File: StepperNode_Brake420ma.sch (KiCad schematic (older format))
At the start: 2 parts

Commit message: Update gimbal and brake MLP position sensor interfaces
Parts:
- added C? (x2): 100nF, symbol C
- added C? (x2): 1uF, symbol C
- added D? (x2): 1N4148, symbol D
- added U? (x2): RCV420JP, symbol RCV420JP
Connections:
- net labels added: +24V_A, BRAKE_MLP1_420MA, BRAKE_MLP2_420MA, GNDA
- wire segments 0 -> 20
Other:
- note added: "Original Author: SafetyLok"
- note added: "rLoop - Stepper Node\nBrake MLP 4-20 Interface\n"

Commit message: Update DAC's and routed gimbal position to MCU direct.
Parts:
- removed C? (x2): 100nF, symbol C
- removed C? (x2): 1uF, symbol C
- removed U? (x2): RCV420JP, symbol RCV420JP
- added C? (x2): C_100nF_50V, RLOOP_FOOTPRINTS:rLoop_C_0603, symbol C_100nF_50V
- added C? (x2): C_1uF_50V, RLOOP_FOOTPRINTS:rLoop_C_0603, symbol C_1uF_50V
- added R? (x2): 1.7K, RLOOP_FOOTPRINTS:rLoop_R_0603, symbol 1.7K
- added R? (x2): 3.3K, RLOOP_FOOTPRINTS:rLoop_R_0603, symbol 3.3K
- added U? (x2): RCV420JP, symbol RCV420JP
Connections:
- net labels added: BRAKE1_MLP_3V
- net labels removed: BRAKE1_MLP, BRAKE2_MLP
- wire segments 20 -> 22

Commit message: First Revision -
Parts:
- removed D? (x2): 1N4148, symbol D
- removed P? (x2): CONN_01X04-2XMNT, symbol CONN_01X04-2XMNT
- added D3, D4: BZX84C3V6LT1G, RLOOP_FOOTPRINTS:rLoop_SOT23, symbol BZX84C3V6LT1G
- added D5, D6: BAS16,215, RLOOP_FOOTPRINTS:rLoop_SOT23, symbol BAS16,215
- added P12: TE_640456-8, RLOOP_FOOTPRINTS:rLoop_TE640456-8, symbol TE_640456-8
- gave numbers to parts that had none: 10
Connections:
- net labels added: BRAKE2_MLP_3V
- wire segments 22 -> 25
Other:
- note added: "LHS/RHS Brake Interface Board\n4-20ma"
- note removed: "LHS Brake Interface Board\n4-20ma"
- note removed: "RHS Brake Interface Board\n4-20ma"

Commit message: Update per design review.
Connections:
- wire segments 25 -> 30
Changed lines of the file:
@@
 Wire Wire Line
 	10700 2600 11350 2600
+$Comp
+L GNDA #PWR?
+U 1 1 575D1FD8
+P 11300 3300
+F 0 "#PWR?" H 11300 3050 50  0001 C CNN
+F 1 "GNDA" H 11300 3150 50  0000 C CNN
+F 2 "" H 11300 3300 50  0000 C CNN
+F 3 "" H 11300 3300 50  0000 C CNN
+	1    11300 3300
+	1    0    0    -1
+$EndComp
+Wire Wire Line
+	11350 2800 11300 2800
+Wire Wire Line
+	11300 2800 11300 3300
+Wire Wire Line
+	11350 3100 11300 3100
+Connection ~ 11300 3100
+Wire Wire Line
+	11350 3000 11300 3000
+Connection ~ 11300 3000
+Wire Wire Line
+	11350 2900 11300 2900
+Connection ~ 11300 2900
 $EndSCHEMATC

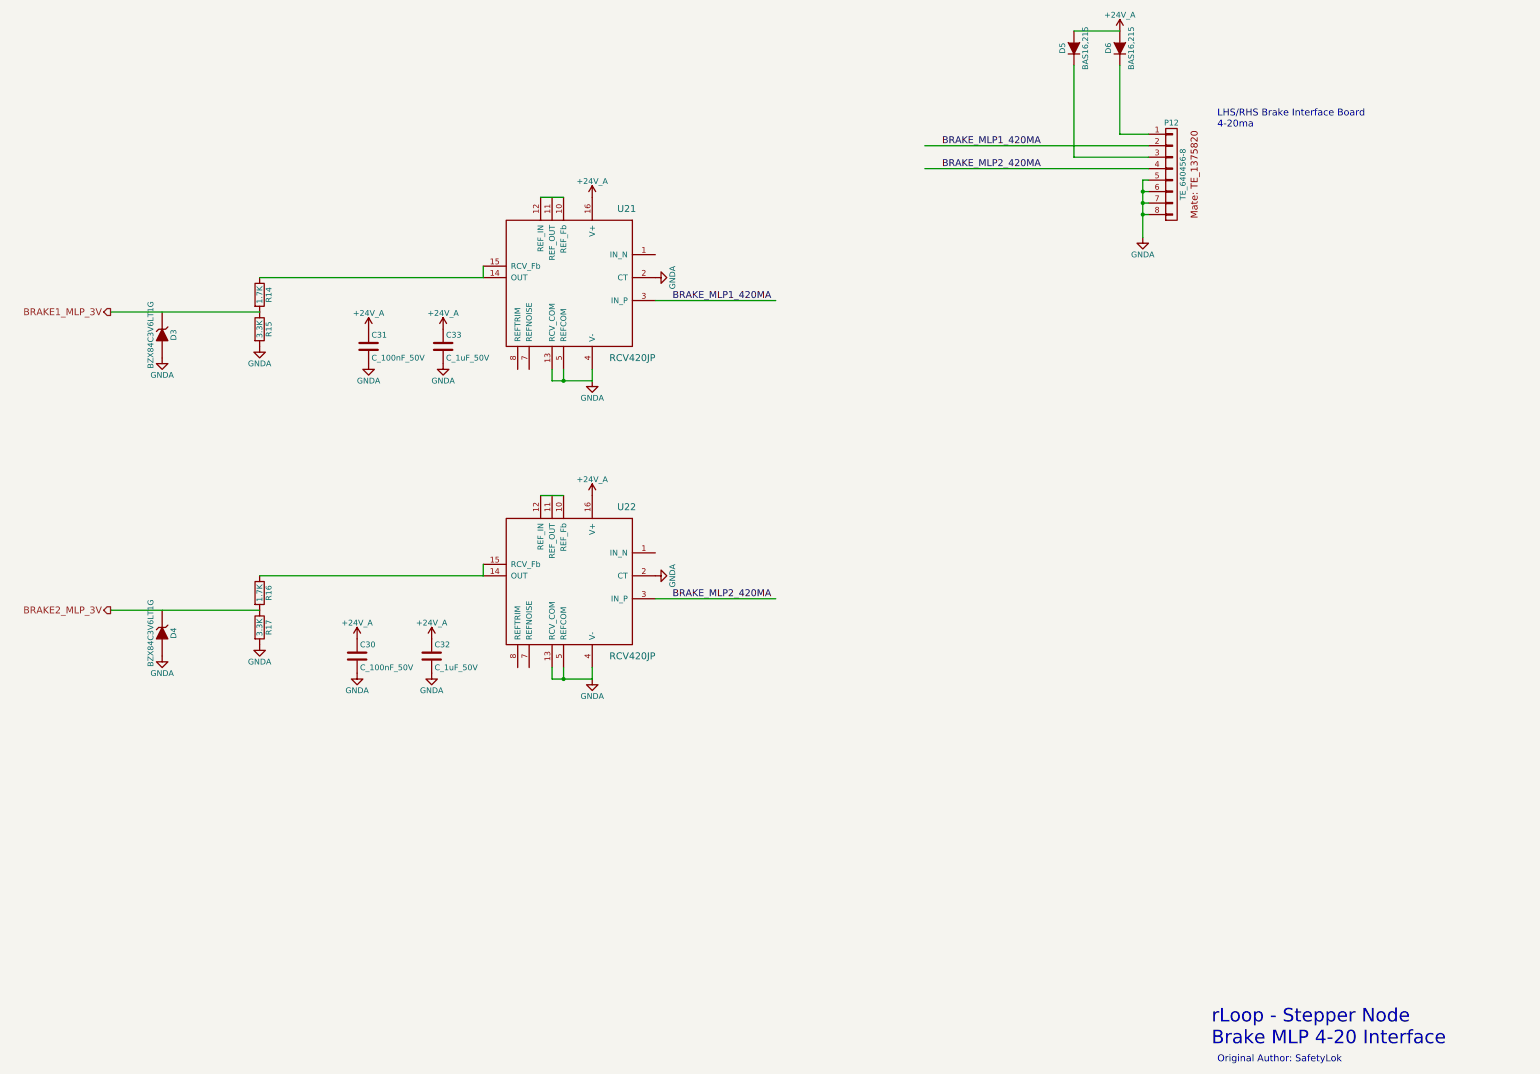
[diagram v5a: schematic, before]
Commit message: Fix most ERC warnings (non-connected pins, etc)
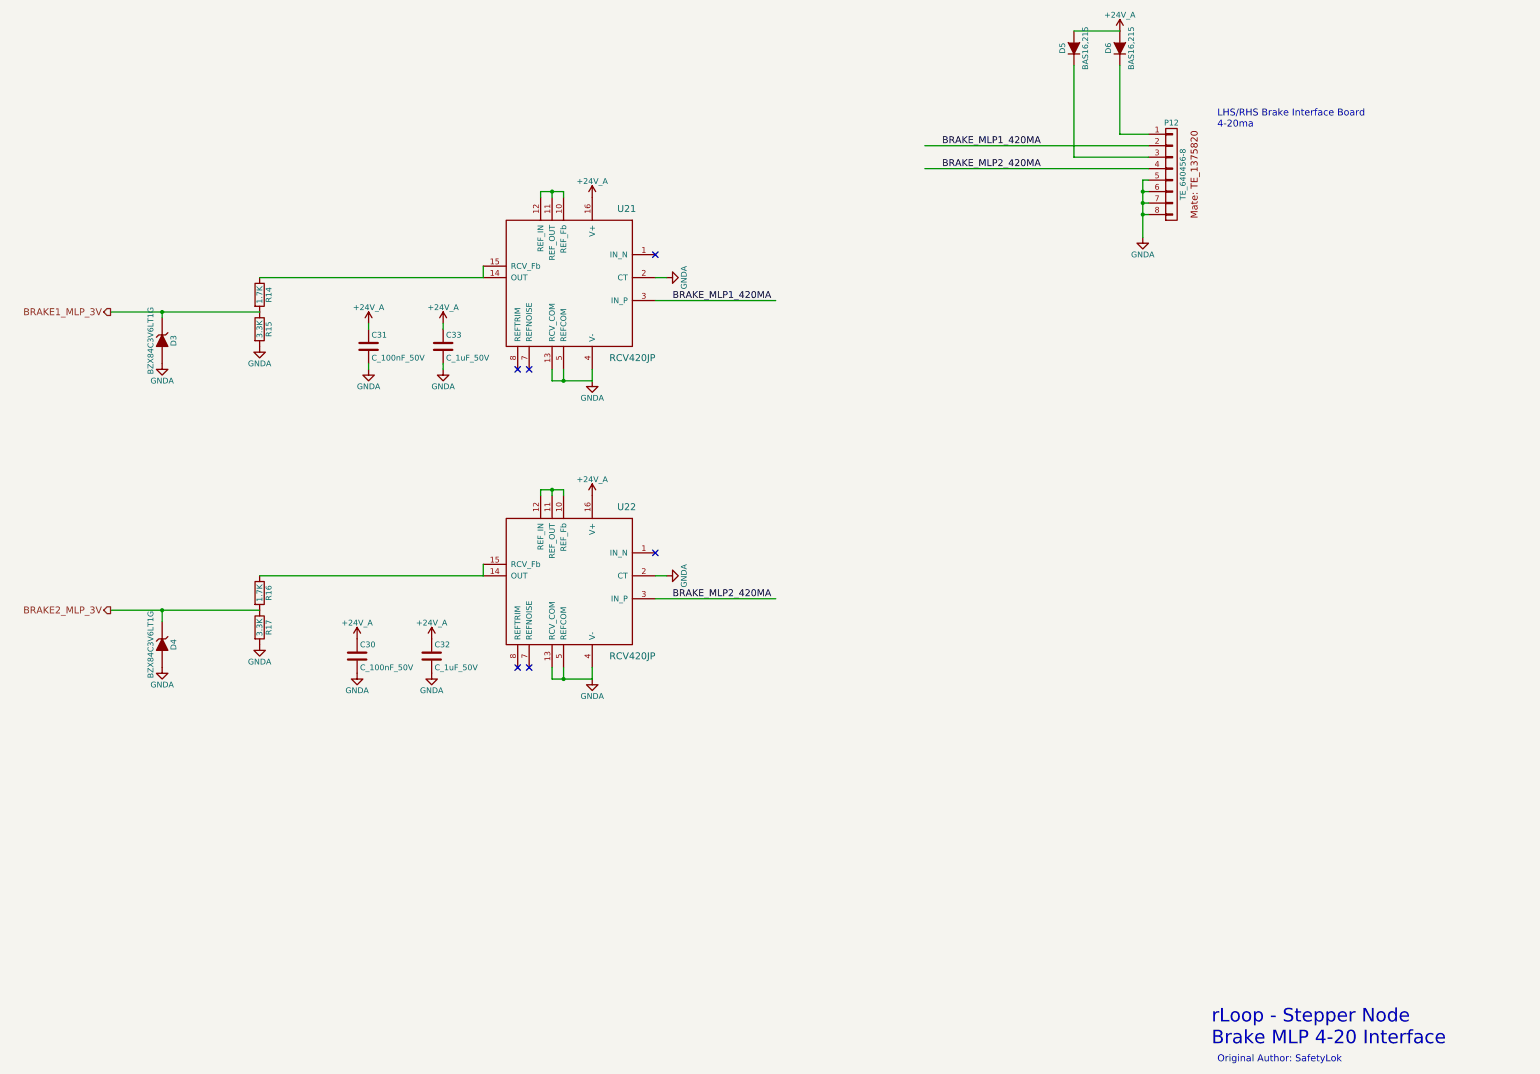
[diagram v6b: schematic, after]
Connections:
- wire segments 30 -> 44
- no-connect marks 0 -> 6
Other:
- moved on the sheet: D3, D4
